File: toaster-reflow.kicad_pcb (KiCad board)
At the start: 2 copper layers, 40.1 x 51.8 mm, 41 parts, among them J1 1935161, J2 1935161, J3 Raspberry_Pi_2_3, J4 Conn_01x04, J6 Conn_01x03, K1 1-1415899-3, Q1 Q_NMOS_GSD, Q2 Q_NMOS_GSD, Q3 Q_PNP_BEC, Q4 Q_PNP_BEC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

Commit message: updates
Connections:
- U2 pad 2: Net-(C3-Pad2) -> /Thermocouple1/T-
- U3 pad 2: Net-(C8-Pad2) -> /Thermocouple2/T-
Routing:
- net Net-(C8-Pad2): track 32.5 -> 15.1 mm
- net Net-(C3-Pad2): track 33.5 -> 18.4 mm
- net /Thermocouple2/T-: track 3.88 -> 14.3 mm
- net /Thermocouple1/T-: track 6.42 -> 15.4 mm
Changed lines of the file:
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@@
     (thickness 1.6)
     (drawings 35)
-    (tracks 548)
+    (tracks 544)
     (zones 0)
     (modules 41)
@@
       (net 4 "Net-(C3-Pad2)"))
     (pad 2 smd rect (at -2.95 1.3) (size 1.45 0.45) (layers B.Cu B.Paste B.Mask)
-      (net 4 "Net-(C3-Pad2)"))
+      (net 48 /Thermocouple1/T-))
     (pad 1 smd rect (at -2.95 1.95) (size 1.45 0.45) (layers B.Cu B.Paste B.Mask)
       (net 2 GND))
@@
       (net 8 "Net-(C8-Pad2)"))
     (pad 2 smd rect (at -2.95 1.3) (size 1.45 0.45) (layers B.Cu B.Paste B.Mask)
-      (net 8 "Net-(C8-Pad2)"))
+      (net 46 /Thermocouple2/T-))
     (pad 1 smd rect (at -2.95 1.95) (size 1.45 0.45) (layers B.Cu B.Paste B.Mask)
       (net 2 GND))
@@
   (segment (start 138.612001 116.095001) (end 138.487 116.22) (width 0.25) (layer B.Cu) (net 4))
   (segment (start 138.612001 113.094999) (end 138.612001 116.095001) (width 0.25) (layer B.Cu) (net 4))
-  (segment (start 127.34201 112.07651) (end 126.492 111.2265) (width 0.25) (layer B.Cu) (net 4) (status 20))
-  (segment (start 127.34201 114.966216) (end 127.34201 112.07651) (width 0.25) (layer B.Cu) (net 4))
-  (segment (start 129.245794 116.87) (end 127.34201 114.966216) (width 0.25) (layer B.Cu) (net 4))
-  (segment (start 137.512 116.87) (end 129.245794 116.87) (width 0.25) (layer B.Cu) (net 4) (status 10))
   (segment (start 128.7525 110.998) (end 128.524 111.2265) (width 0.25) (layer B.Cu) (net 4) (status 30))
   (segment (start 132.3085 110.998) (end 128.7525 110.998) (width 0.25) (layer B.Cu) (net 4) (status 30))
@@
   (segment (start 134.366 99.822) (end 143.002 108.458) (width 0.25) (layer F.Cu) (net 6))
   (segment (start 143.002 108.458) (end 144.526 108.458) (width 0.25) (layer F.Cu) (net 6))
-  (segment (start 144.526 110.166) (end 144.202 110.49) (width 0.25) (layer B.Cu) (net 10) (status 30))
   (segment (start 156.972 74.93) (end 155.872 74.93) (width 0.25) (layer B.Cu) (net 6) (status 10))
   (segment (start 140.607999 92.818001) (end 140.208 93.218) (width 0.25) (layer F.Cu) (net 6))
@@
   (segment (start 152.324 86.436) (end 155.194 83.566) (width 0.25) (layer B.Cu) (net 6))
   (segment (start 152.324 89.078) (end 152.324 86.436) (width 0.25) (layer B.Cu) (net 6))
+  (segment (start 141.802 109.54) (end 141.811199 109.54) (width 0.25) (layer B.Cu) (net 6) (status 30))
+  (segment (start 150.504 121.666) (end 150.438 121.732) (width 0.25) (layer B.Cu) (net 6) (status 30))
+  (segment (start 150.438 121.082) (end 150.438 121.732) (width 0.25) (layer B.Cu) (net 6))
+  (segment (start 151.61802 119.90198) (end 150.438 121.082) (width 0.25) (layer B.Cu) (net 6))
+  (segment (start 151.61802 116.82002) (end 151.61802 119.90198) (width 0.25) (layer B.Cu) (net 6))
+  (segment (start 150.114 115.316) (end 151.61802 116.82002) (width 0.25) (layer B.Cu) (net 6))
+  (segment (start 145.796 112.247315) (end 145.796 112.813) (width 0.25) (layer B.Cu) (net 6))
+  (segment (start 145.796 110.293685) (end 145.796 112.247315) (width 0.25) (layer B.Cu) (net 6))
+  (segment (start 144.526 109.023685) (end 145.796 110.293685) (width 0.25) (layer B.Cu) (net 6))
+  (segment (start 144.526 108.458) (end 144.526 109.023685) (width 0.25) (layer B.Cu) (net 6))
+  (segment (start 143.444 109.54) (end 144.526 108.458) (width 0.25) (layer B.Cu) (net 6))
+  (segment (start 141.802 109.54) (end 143.444 109.54) (width 0.25) (layer B.Cu) (net 6))
   (segment (start 125.2475 119.634) (end 125.2475 117.348) (width 0.25) (layer B.Cu) (net 7) (status 30))
   (segment (start 131.639499 119.287001) (end 132.5625 118.364) (width 0.25) (layer B.Cu) (net 7) (status 20))
@@
   (segment (start 123.6725 120.091) (end 123.6725 119.634) (width 0.25) (layer B.Cu) (net 8) (status 30))
   (segment (start 125.222 121.6405) (end 123.6725 120.091) (width 0.25) (layer B.Cu) (net 8) (status 30))
-  (segment (start 137.512 122.712) (end 136.622 122.712) (width 0.25) (layer B.Cu) (net 8) (status 10))
+  (segment (start 137.512 122.712) (end 136.622 122.712) (width 0.25) (layer B.Cu) (net 46) (status 10))
   (segment (start 137.471888 122.102112) (end 137.512 122.062) (width 0.25) (layer B.Cu) (net 8) (status 30))
   (segment (start 132.287612 122.102112) (end 137.471888 122.102112) (width 0.25) (layer B.Cu) (net 8) (status 20))
   (segment (start 131.826 121.6405) (end 132.287612 122.102112) (width 0.25) (layer B.Cu) (net 8) (status 10))
-  (segment (start 124.978795 124.287001) (end 134.030999 124.287001) (width 0.25) (layer B.Cu) (net 8))
-  (segment (start 135.606 122.712) (end 137.512 122.712) (width 0.25) (layer B.Cu) (net 8) (status 20))
-  (segment (start 124.37199 123.680196) (end 124.978795 124.287001) (width 0.25) (layer B.Cu) (net 8))
-  (segment (start 125.222 121.6405) (end 124.37199 122.49051) (width 0.25) (layer B.Cu) (net 8) (status 10))
-  (segment (start 134.030999 124.287001) (end 135.606 122.712) (width 0.25) (layer B.Cu) (net 8))
-  (segment (start 124.37199 122.49051) (end 124.37199 123.680196) (width 0.25) (layer B.Cu) (net 8))
+  (segment (start 135.606 122.712) (end 137.512 122.712) (width 0.25) (layer B.Cu) (net 46) (status 20))
+  (segment (start 134.030999 124.287001) (end 135.606 122.712) (width 0.25) (layer B.Cu) (net 46))
   (segment (start 127.0255 88.9) (end 130.7845 88.9) (width 0.25) (layer F.Cu) (net 9) (status 30))
+  (segment (start 144.526 110.166) (end 144.202 110.49) (width 0.25) (layer B.Cu) (net 10) (status 30))
   (via (at 142.732778 110.461579) (size 0.8) (drill 0.4) (layers F.Cu B.Cu) (net 10))
-  (segment (start 141.802 109.54) (end 141.811199 109.54) (width 0.25) (layer B.Cu) (net 6) (status 30))
   (segment (start 135.418999 114.446999) (end 135.418999 115.606999) (width 0.25) (layer F.Cu) (net 10))
   (segment (start 142.732778 110.461579) (end 139.404419 110.461579) (width 0.25) (layer F.Cu) (net 10))
@@
   (segment (start 135.8645 116.0525) (end 137.668 116.0525) (width 0.25) (layer F.Cu) (net 10) (status 20))
   (segment (start 135.418999 115.606999) (end 135.8645 116.0525) (width 0.25) (layer F.Cu) (net 10))
-  (via (at 151.892 121.666) (size 0.8) (drill 0.4) (layers F.Cu B.Cu) (net 11))
-  (segment (start 150.504 121.666) (end 150.438 121.732) (width 0.25) (layer B.Cu) (net 6) (status 30))
-  (segment (start 150.438 121.082) (end 150.438 121.732) (width 0.25) (layer B.Cu) (net 6))
-  (segment (start 151.61802 119.90198) (end 150.438 121.082) (width 0.25) (layer B.Cu) (net 6))
-  (segment (start 151.61802 116.82002) (end 151.61802 119.90198) (width 0.25) (layer B.Cu) (net 6))
-  (segment (start 150.114 115.316) (end 151.61802 116.82002) (width 0.25) (layer B.Cu) (net 6))
-  (segment (start 145.796 112.247315) (end 145.796 112.813) (width 0.25) (layer B.Cu) (net 6))
-  (segment (start 145.796 110.293685) (end 145.796 112.247315) (width 0.25) (layer B.Cu) (net 6))
-  (segment (start 144.526 109.023685) (end 145.796 110.293685) (width 0.25) (layer B.Cu) (net 6))
-  (segment (start 144.526 108.458) (end 144.526 109.023685) (width 0.25) (layer B.Cu) (net 6))
-  (segment (start 143.444 109.54) (end 144.526 108.458) (width 0.25) (layer B.Cu) (net 6))
-  (segment (start 141.802 109.54) (end 143.444 109.54) (width 0.25) (layer B.Cu) (net 6))
   (segment (start 142.761199 110.49) (end 142.732778 110.461579) (width 0.25) (layer B.Cu) (net 10))
   (segment (start 144.202 110.49) (end 142.761199 110.49) (width 0.25) (layer B.Cu) (net 10))
+  (via (at 151.892 121.666) (size 0.8) (drill 0.4) (layers F.Cu B.Cu) (net 11))
   (segment (start 150.134888 123.423112) (end 151.892 121.666) (width 0.25) (layer F.Cu) (net 11))
   (segment (start 137.668 122.9615) (end 138.129612 123.423112) (width 0.25) (layer F.Cu) (net 11) (status 10))
@@
   (segment (start 125.2875 123.15) (end 125.222 123.2155) (width 0.25) (layer B.Cu) (net 46) (status 30))
   (segment (start 129.072 123.15) (end 125.2875 123.15) (width 0.25) (layer B.Cu) (net 46) (status 30))
+  (segment (start 130.209001 124.287001) (end 129.072 123.15) (width 0.25) (layer B.Cu) (net 46))
+  (segment (start 134.030999 124.287001) (end 130.209001 124.287001) (width 0.25) (layer B.Cu) (net 46))
   (segment (start 134.072 118.4295) (end 134.1375 118.364) (width 0.25) (layer B.Cu) (net 47) (status 30))
   (segment (start 134.072 120.65) (end 134.072 118.4295) (width 0.25) (layer B.Cu) (net 47) (status 30))
   (segment (start 126.492 115.57) (end 126.492 112.8015) (width 0.25) (layer B.Cu) (net 48) (status 20))
   (segment (start 129.072 118.15) (end 126.492 115.57) (width 0.25) (layer B.Cu) (net 48) (status 10))
+  (segment (start 130.352 116.87) (end 129.072 118.15) (width 0.25) (layer B.Cu) (net 48))
+  (segment (start 137.512 116.87) (end 130.352 116.87) (width 0.25) (layer B.Cu) (net 48))
   (segment (start 130.9155 115.65) (end 130.0735 114.808) (width 0.25) (layer B.Cu) (net 49) (status 20))
   (segment (start 134.072 115.65) (end 130.9155 115.65) (width 0.25) (layer B.Cu) (net 49) (status 10))

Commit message: update some stuff
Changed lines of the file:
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@@
-(kicad_pcb (version 20171130) (host pcbnew 5.0.0)
+(kicad_pcb (version 20171130) (host pcbnew 5.0.1)
   (general
     (thickness 1.6)
@@
     (pad_drill 0.762)
     (pad_to_mask_clearance 0.2)
+    (solder_mask_min_width 0.25)
     (aux_axis_origin 0 0)
     (visible_elements FFFFFF7F)
     (pcbplotparams
-      (layerselection 0x010fc_ffffffff)
+      (layerselection 0x010ff_ffffffff)
       (usegerberextensions false)
       (usegerberattributes false)
@@
       (outputformat 1)
       (mirror false)
-      (drillshape 1)
+      (drillshape 0)
       (scaleselection 1)
-      (outputdirectory ""))
+      (outputdirectory "gerbers"))
   )
   (net 0 "")
@@
       (effects (font (size 1.00198 1.00198) (thickness 0.05)))
     )
-    (fp_circle (center -15.5 3.75) (end -15.2 3.75) (layer F.SilkS) (width 0))
+    (fp_circle (center -15.5 3.75) (end -15.2 3.75) (layer F.SilkS) (width 0.1))
     (fp_line (start -14.75 6.6) (end -14.75 -6.6) (layer Eco1.User) (width 0.05))
     (fp_line (start 14.75 6.6) (end -14.75 6.6) (layer Eco1.User) (width 0.05))
@@
     (pad 1 thru_hole rect (at 0 0) (size 1.7 1.7) (drill 1) (layers *.Cu *.Mask)
       (net 6 +3V3))
-    (model ${KISYS3DMOD}/Connector_PinHeader_2.54mm.3dshapes/PinHeader_2x20_P2.54mm_Vertical.wrl
-      (at (xyz 0 0 0))
-      (scale (xyz 1 1 1))
-      (rotate (xyz 0 0 0))
-    )
     (model ${KIPRJMOD}/kicad-packages3D/Connector_PinSocket_2.54mm.3dshapes/PinSocket_2x20_P2.54mm_Vertical.wrl
       (offset (xyz 0 0 -1.6))
@@
   (segment (start 123.6725 120.091) (end 123.6725 119.634) (width 0.25) (layer B.Cu) (net 8) (status 30))
   (segment (start 125.222 121.6405) (end 123.6725 120.091) (width 0.25) (layer B.Cu) (net 8) (status 30))
-  (segment (start 137.512 122.712) (end 136.622 122.712) (width 0.25) (layer B.Cu) (net 46) (status 10))
   (segment (start 137.471888 122.102112) (end 137.512 122.062) (width 0.25) (layer B.Cu) (net 8) (status 30))
   (segment (start 132.287612 122.102112) (end 137.471888 122.102112) (width 0.25) (layer B.Cu) (net 8) (status 20))
   (segment (start 131.826 121.6405) (end 132.287612 122.102112) (width 0.25) (layer B.Cu) (net 8) (status 10))
-  (segment (start 135.606 122.712) (end 137.512 122.712) (width 0.25) (layer B.Cu) (net 46) (status 20))
-  (segment (start 134.030999 124.287001) (end 135.606 122.712) (width 0.25) (layer B.Cu) (net 46))
   (segment (start 127.0255 88.9) (end 130.7845 88.9) (width 0.25) (layer F.Cu) (net 9) (status 30))
   (segment (start 144.526 110.166) (end 144.202 110.49) (width 0.25) (layer B.Cu) (net 10) (status 30))
@@
   (segment (start 133.35 97.224315) (end 133.096 96.970315) (width 0.25) (layer B.Cu) (net 45))
   (segment (start 133.35 97.79) (end 133.35 97.224315) (width 0.25) (layer B.Cu) (net 45))
+  (segment (start 137.512 122.712) (end 136.622 122.712) (width 0.25) (layer B.Cu) (net 46) (status 10))
+  (segment (start 135.606 122.712) (end 137.512 122.712) (width 0.25) (layer B.Cu) (net 46) (status 20))
+  (segment (start 134.030999 124.287001) (end 135.606 122.712) (width 0.25) (layer B.Cu) (net 46))
   (segment (start 125.2875 123.15) (end 125.222 123.2155) (width 0.25) (layer B.Cu) (net 46) (status 30))
   (segment (start 129.072 123.15) (end 125.2875 123.15) (width 0.25) (layer B.Cu) (net 46) (status 30))

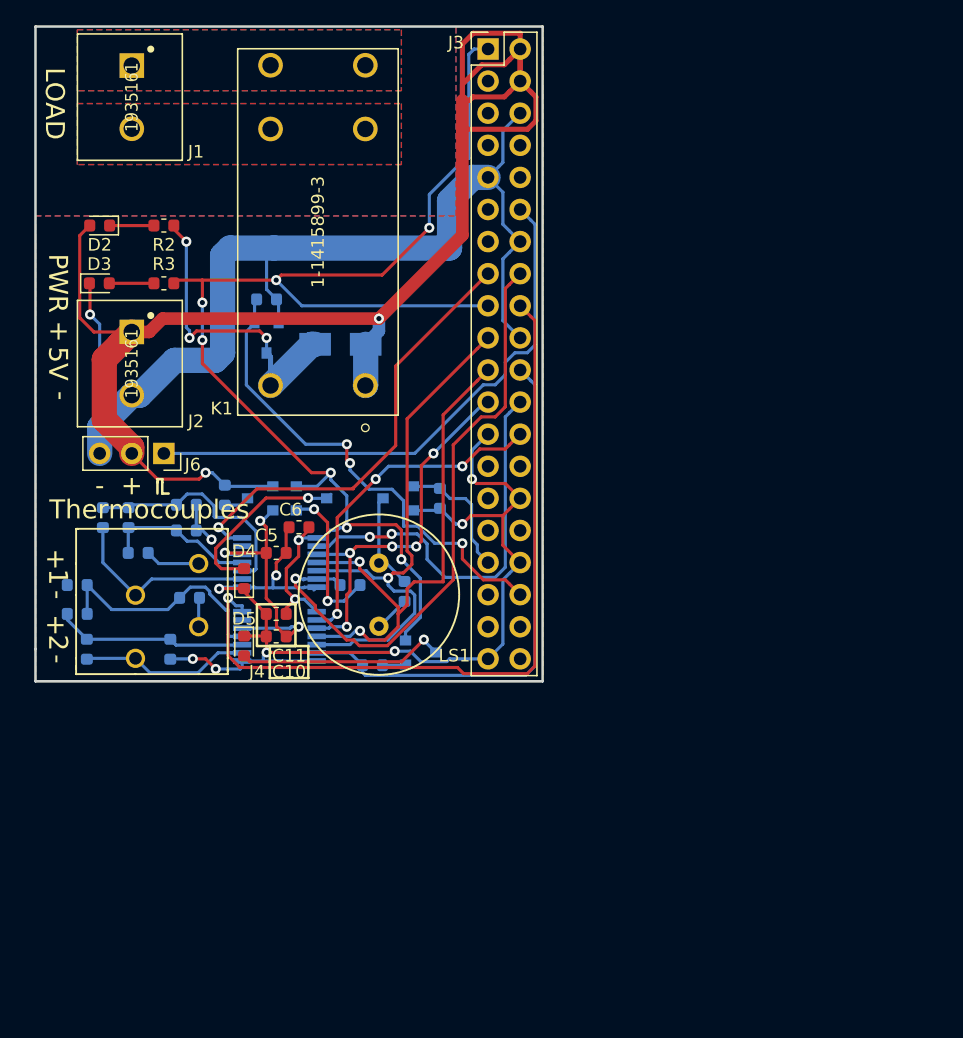
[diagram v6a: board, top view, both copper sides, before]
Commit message: new design/ layout
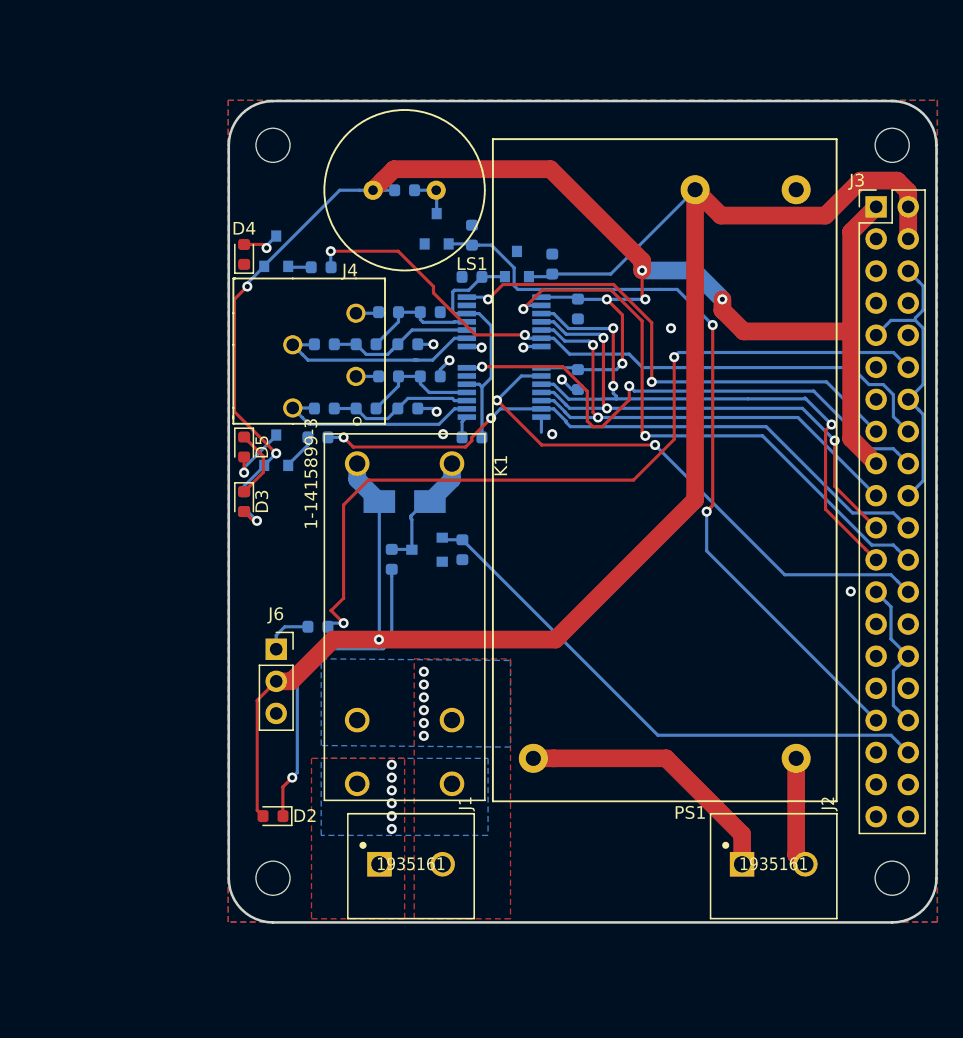
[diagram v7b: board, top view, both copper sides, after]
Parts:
- added MH1: MountingHole, MountingHole:MountingHole_2.7mm_M2.5, F.Cu at (140.0, 82.5)
- added MH2: MountingHole, MountingHole:MountingHole_2.7mm_M2.5, F.Cu at (189.0, 140.6)
- added MH3: MountingHole, MountingHole:MountingHole_2.7mm_M2.5, F.Cu at (140.0, 140.6)
- added MH4: MountingHole, MountingHole:MountingHole_2.7mm_M2.5, F.Cu at (189.0, 82.5)
- added PS1: IRM-02-9, custom:IRM-15-5, F.Cu at (181.4, 131.1)
- added R12: 1K, Resistor_SMD:R_0603_1608Metric, B.Cu at (143.5, 120.7)
- C10, C11, C5, C6, R2, R3: moved to B.Cu
- moved J1 64.6 mm to (150.9, 139.4), turned to 0 degrees
- moved J2 64.4 mm to (179.6, 139.4), turned to 0 degrees
- moved D2 48.7 mm to (140.0, 135.6)
- moved C11 33.9 mm to (164.1, 95.5), turned to 270 degrees
- moved J3 33.2 mm to (187.7, 87.4)
- moved C7 32.5 mm to (152.4, 100.8), turned to 180 degrees
- moved C10 32.4 mm to (155.7, 93.0)
- moved LS1 32.1 mm to (150.4, 86.1), turned to 0 degrees
- moved R2 32.0 mm to (149.4, 115.3), turned to 270 degrees
- moved R5 31.8 mm to (150.4, 86.1), turned to 0 degrees
- moved C1 31.7 mm to (162.1, 91.9), turned to 270 degrees
- moved K1 31.2 mm to (150.4, 119.9), turned to 270 degrees
- moved C8 28.1 mm to (147.3, 103.4)
- moved U1 27.5 mm to (159.3, 91.9), turned to 90 degrees
- moved R6 27.5 mm to (149.1, 95.8), turned to 180 degrees
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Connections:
- J2 pad 1: +5V -> Net-(J2-Pad1)
- J2 pad 2: GND -> Net-(J2-Pad2)
- J6 pad 1: /SERVO_PWM -> Net-(J6-Pad1)
- LS1 pad 1: Net-(LS1-Pad1) -> +3V3
- R5 pad 1: Net-(LS1-Pad1) -> +3V3
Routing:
- net GND: track 180.9 -> 53.3 mm
- net /BUZZER: track 10.3 -> 62.0 mm, vias 0 -> 2
- net Net-(D2-Pad1): track 3.76 -> 26.1 mm, vias 0 -> 1
- net Net-(J2-Pad1): track 0.00 -> 21.4 mm
- net /SERVO_PWM: track 44.7 -> 65.6 mm, vias 0 -> 2
- net /THERMO_SCK: track 30.4 -> 48.9 mm, vias 5 -> 3
- net /THERMO2_DRDY: track 60.5 -> 42.8 mm, vias 1 -> 2
- net /THERMO2_CS: track 26.7 -> 43.1 mm, vias 3 -> 2
- net /THERMO1_CS: track 31.4 -> 46.6 mm
- net Net-(D1-Pad2): track 24.7 -> 10.0 mm, vias 3 -> 0
- net Net-(D4-Pad2): track 14.5 -> 3.16 mm
- net Net-(D5-Pad2): track 16.6 -> 5.27 mm
- net Net-(Q3-Pad1): track 12.3 -> 1.85 mm, vias 2 -> 0
- net +3V3: track 114.3 -> 123.8 mm, vias 9 -> 7
- net Net-(C7-Pad2): track 19.0 -> 9.55 mm
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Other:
- board size 40.1 x 51.8 mm -> 56 x 65 mm
- net class 3A removed
- net class AC_Load removed
- net class THERMOCOUPLE removed
- rule pad_to_mask_clearance: 0.2 -> 0
- board text removed: "+"
- board text removed: "-"
- board text removed: "1"
- board text removed: "2"
- board text removed: "5V"
- board text removed: "LOAD"
- board text removed: "PWR"
- board text removed: "Thermocouples"

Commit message: update some silkscreening
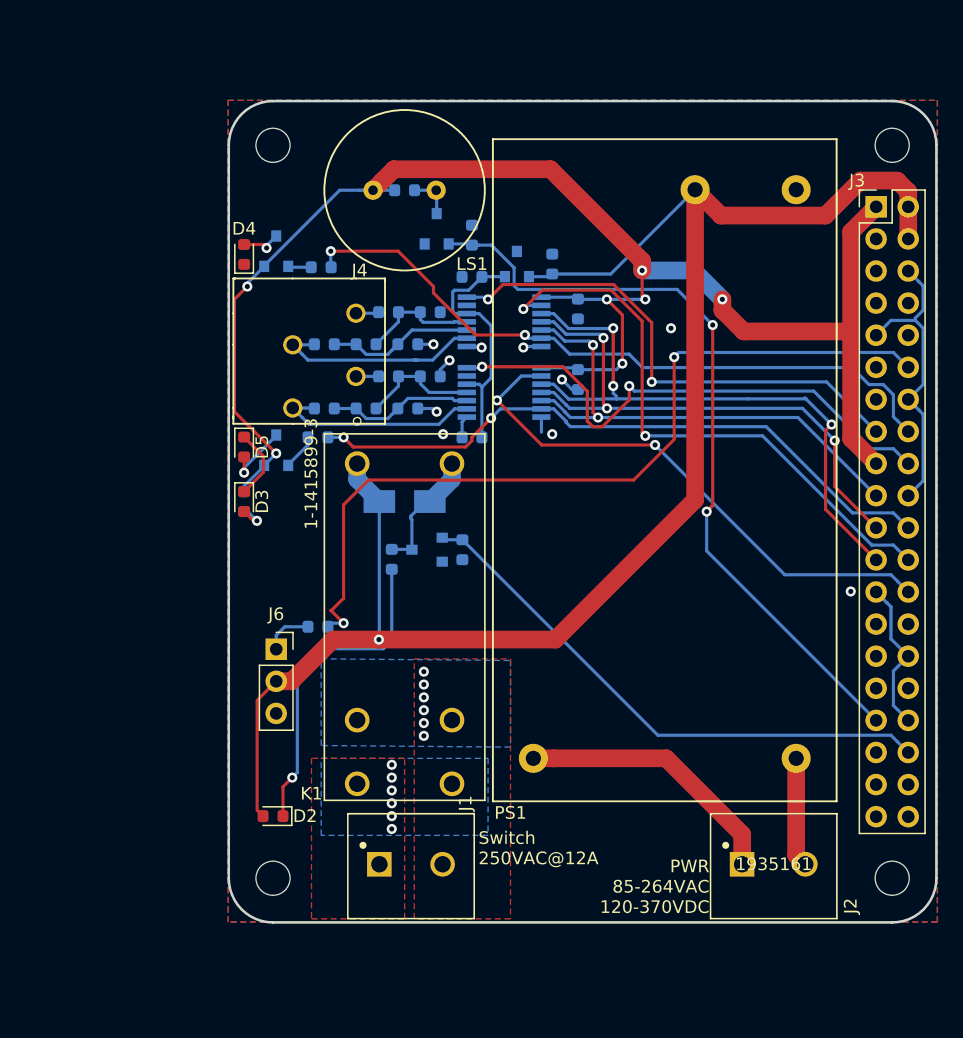
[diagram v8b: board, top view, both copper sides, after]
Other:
- board text added: "PWR 85-264VAC 120-370VDC"
- board text added: "Switch 250VAC@12A"
